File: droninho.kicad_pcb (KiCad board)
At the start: 2 copper layers, 48 x 81.6 mm, 22 parts, among them J1 Conn_01x02_Pin, J2 M2, J3 M1, J4 M3, J5 M4, J6 I2C, J7 TXD0/RXD0, J8 I2C, Q1 SI2300, Q2 SI2300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

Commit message: Ready for review.
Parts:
- removed U3: MPU9250/6500, Library:MPU-9250-6500
- added U4: MPU9250/6500, Library:MPU-9250-6500, F.Cu at (132.1, 136.1)
- J6, J7, J8: footprint Connector:FanPinHeader_1x04_P2.54mm_Vertical -> Connector_PinHeader_2.54mm:PinHeader_1x04_P2.54mm_Vertical
- moved J6 1.51 mm to (127.7, 97.9), turned to 0 degrees
- moved J8 0.93 mm to (162.9, 112.3), turned to 180 degrees
- moved J7 0.89 mm to (162.9, 99.4), turned to 180 degrees
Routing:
- net /SDA: track 89.3 -> 85.4 mm
- net +3.3V: track 215.0 -> 216.1 mm
- net /SCL: track 94.7 -> 93.8 mm
- net GND: track 128.7 -> 129.5 mm
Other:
- board text added: "+3.3v"
- board text added: "- +"
- board text added: "3.3v"
- board text added: "ESP32-DevKit"
- board text added: "GND"
- board text added: "M1"
- board text added: "M2"
- board text added: "M3"
- board text added: "M4"
- board text added: "RX0"
- board text added: "RX2"
- board text added: "RXD2"
- board text added: "SCL"
- board text added: "SDA"
- board text added: "TX0"
- board text added: "TX2"
- board text added: "TXD2"

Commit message: small changes
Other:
- board text removed: "RXD2"
- board text removed: "TXD2"
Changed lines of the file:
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@@
 		)
 	)
-	(gr_text "RXD2"
+	(gr_text "RX2"
 		(at 164.65 110.29 0)
 		(layer "F.SilkS")
@@
 		)
 	)
-	(gr_text "TXD2"
+	(gr_text "TX2"
 		(at 164.65 112.92 0)
 		(layer "F.SilkS")

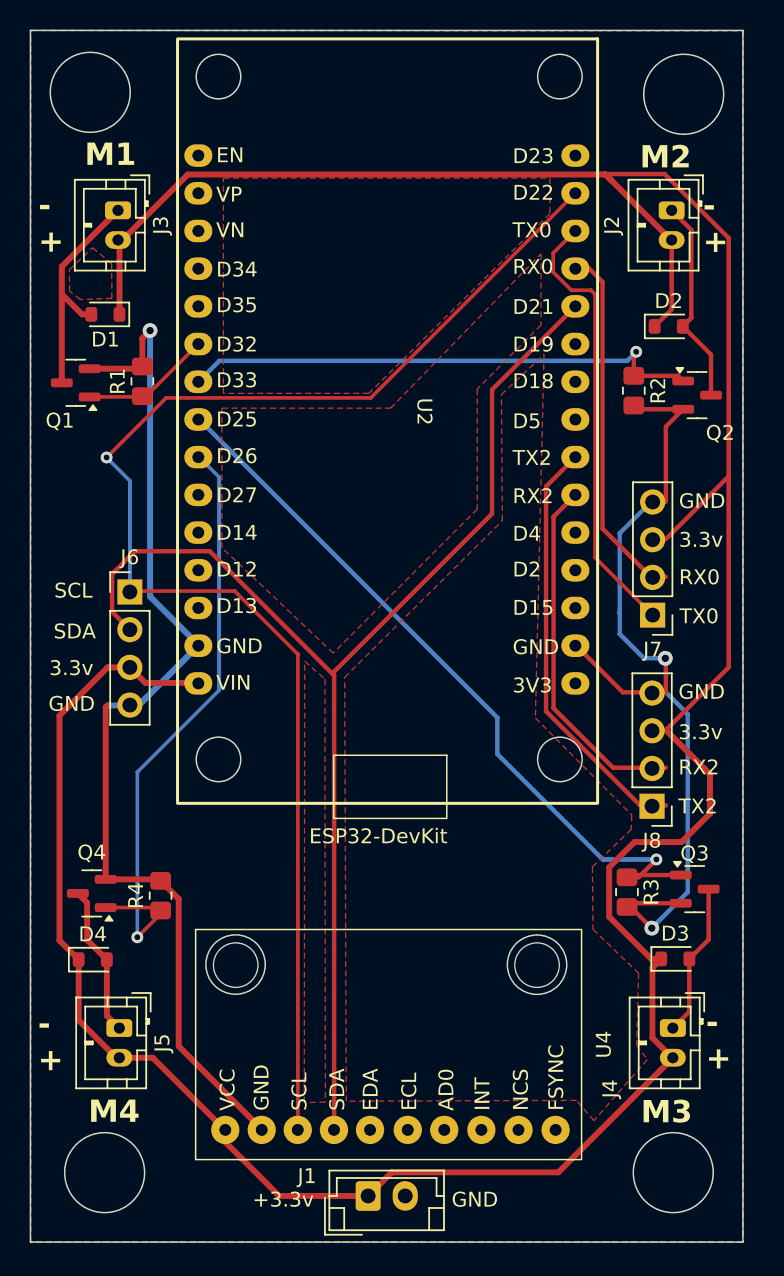
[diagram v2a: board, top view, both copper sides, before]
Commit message: Versão com WIFI de fora da placa.
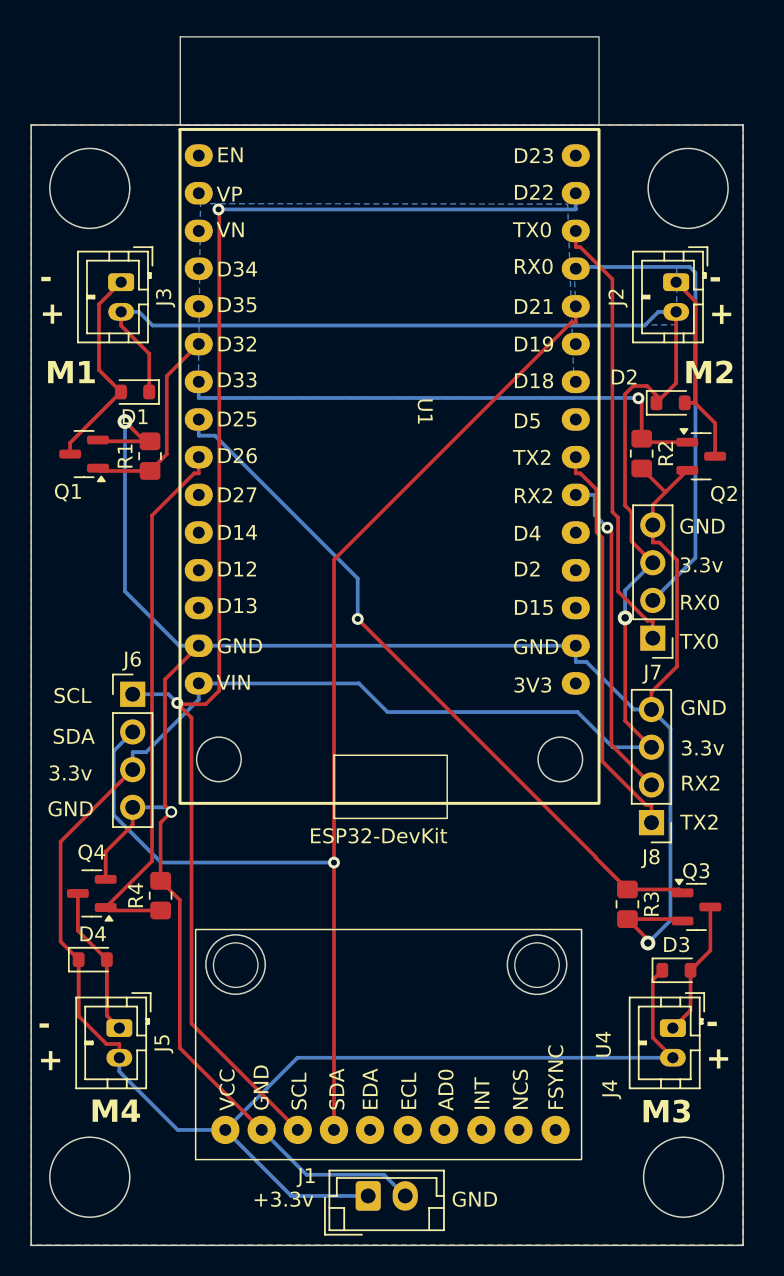
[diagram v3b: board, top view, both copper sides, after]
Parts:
- removed U2: ESP32 Dev Kit, Library:ESP32_30pin
- added U1: ESP32 Dev Kit, Library:ESP32_30pin vertical WIFI, F.Cu at (144.7, 86.2)
- moved J6 6.89 mm to (127.9, 104.8)
- moved D1 5.60 mm to (128.1, 84.4)
- moved D2 5.15 mm to (164.1, 85.1)
- moved R1 5.07 mm to (129.1, 88.7)
- moved J2 4.85 mm to (164.5, 77.0)
- moved J3 4.84 mm to (127.1, 77.0)
- moved Q1 4.83 mm to (124.6, 88.6)
- moved R2 4.27 mm to (162.2, 88.6)
- moved Q2 4.13 mm to (166.2, 88.7)
- moved J7 1.55 mm to (162.9, 101.0)
- moved Q3 1.21 mm to (165.9, 119.1)
- moved J8 1.11 mm to (162.8, 113.4)
- moved R3 0.82 mm to (161.2, 118.9)
- moved D3 0.77 mm to (164.5, 123.4)
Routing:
- net GND: track 129.5 -> 157.3 mm
- net +3.3V: track 216.1 -> 204.3 mm, vias 0 -> 1
- net /RXD0: track 24.4 -> 31.5 mm
- net /PWM1: track 8.84 -> 13.5 mm
- net /PWM4: track 41.5 -> 36.9 mm, vias 1 -> 0
- net /PWM3: track 50.7 -> 48.1 mm
- net /SCL: track 93.8 -> 96.0 mm, vias 1 -> 2
- net /RXD2: track 24.3 -> 22.4 mm, vias 0 -> 1
- net /TXD2: track 28.7 -> 27.1 mm
- net /M1-: track 15.7 -> 14.2 mm
- net /PWM2: track 35.5 -> 36.9 mm
- net /M3-: track 10.4 -> 9.21 mm
- net /SDA: track 85.4 -> 84.7 mm, vias 0 -> 1
- added copper zone on B.Cu, net (none)
- removed copper zone on F.Cu, net (none)
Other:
- board size 48 x 81.6 mm -> 48 x 75.5 mm

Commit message: BOM, DCR e erc OKAY.
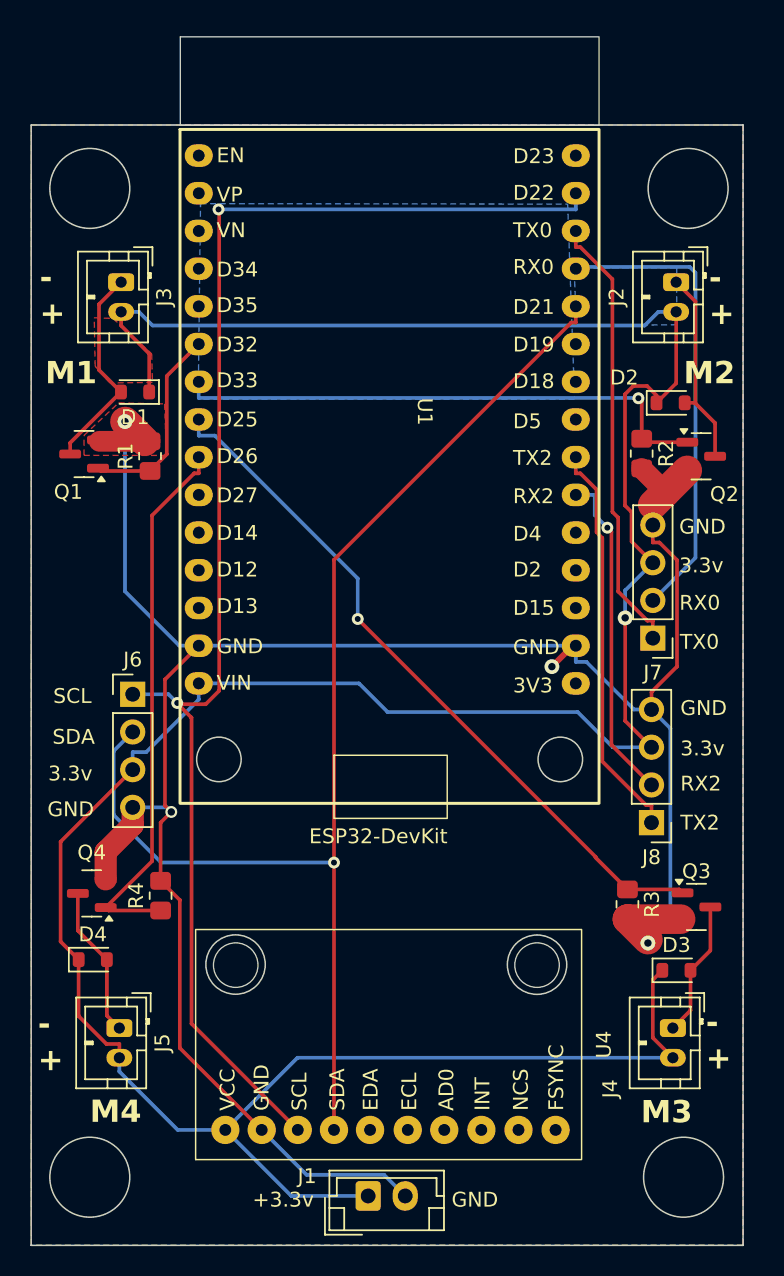
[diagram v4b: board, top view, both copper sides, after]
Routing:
- net GND: track 157.3 -> 159.5 mm, vias 3 -> 4
- added copper zone on F.Cu, net (none)
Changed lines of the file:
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@@
 		(start 162.6 121.3)
 		(end 161.22 119.92)
-		(width 0.25)
+		(width 2)
 		(layer "F.Cu")
 		(net 5)
@@
 		(start 127.89 112.39)
 		(end 127.89 113.5667)
-		(width 0.25)
+		(width 1.5)
 		(layer "F.Cu")
 		(net 5)
@@
 		(start 163.78 91.16)
 		(end 162.18 89.56)
-		(width 0.25)
+		(width 1.4)
 		(layer "F.Cu")
 		(net 5)
@@
 	)
 	(segment
+		(start 157.739987 101.500013)
+		(end 157.76 101.48)
+		(width 0.4)
+		(layer "F.Cu")
+		(net 5)
+	)
+	(segment
 		(start 128.7 87.73)
 		(end 127.37 86.4)
-		(width 0.25)
+		(width 2)
 		(layer "F.Cu")
 		(net 5)
@@
 		(start 125.64 87.73)
 		(end 129.06 87.73)
-		(width 0.25)
+		(width 1.4)
 		(layer "F.Cu")
 		(net 5)
@@
 		(start 127.89 113.5667)
 		(end 126.07 115.3867)
-		(width 0.25)
+		(width 1.5)
 		(layer "F.Cu")
 		(net 5)
@@
 	)
 	(segment
+		(start 157.73996 101.500013)
+		(end 157.539987 101.500013)
+		(width 0.4)
+		(layer "F.Cu")
+		(net 5)
+	)
+	(segment
 		(start 164.5584 95.733863)
 		(end 163.371237 94.5467)
@@
 	)
 	(segment
+		(start 157.73996 101.500013)
+		(end 157.739987 101.500013)
+		(width 0.4)
+		(layer "F.Cu")
+		(net 5)
+	)
+	(segment
 		(start 130.064 103.775973)
 		(end 130.064 112.274)
@@
 		(start 165.25 89.69)
 		(end 163.78 91.16)
-		(width 0.25)
+		(width 2)
 		(layer "F.Cu")
 		(net 5)
@@
 		(start 164.8 119.92)
 		(end 161.22 119.92)
-		(width 0.25)
+		(width 2)
 		(layer "F.Cu")
 		(net 5)
@@
 		(start 163.78 91.16)
 		(end 162.93 92.01)
-		(width 0.25)
+		(width 2)
 		(layer "F.Cu")
 		(net 5)
@@
 		(start 126.07 115.3867)
 		(end 126.07 117.24)
-		(width 0.25)
-		(layer "F.Cu")
+		(width 1.5)
+		(layer "F.Cu")
+		(net 5)
+	)
+	(segment
+		(start 157.539987 101.500013)
+		(end 156.13 102.91)
+		(width 0.4)
+		(layer "F.Cu")
+		(net 5)
+	)
+	(via
+		(at 156.13 102.91)
+		(size 1)
+		(drill 0.5)
+		(layers "F.Cu" "B.Cu")
 		(net 5)
 	)
@@
 	)
 	(zone
+		(net 5)
+		(net_name "GND")
+		(layer "F.Cu")
+		(hatch edge 0.5)
+		(priority 4)
+		(connect_pads
+			(clearance 0.508)
+		)
+		(min_thickness 0.25)
+		(filled_areas_thickness no)
+		(fill yes
+			(thermal_gap 0.5)
+			(thermal_bridge_width 0.5)
+		)
+		(polygon
+			(pts
+				(xy 130.17 88.68) (xy 124.6125 88.6775) (xy 124.6125 87.33) (xy 126.94 85.14) (xy 130.04 85.21)
+			)
+		)
+	)
+	(zone
+		(net 0)
+		(net_name "")
+		(layer "F.Cu")
+		(hatch edge 0.5)
+		(priority 3)
+		(connect_pads
+			(clearance 0.508)
+		)
+		(min_thickness 0.25)
+		(filled_areas_thickness no)
+		(fill yes
+			(thermal_gap 0.5)
+			(thermal_bridge_width 0.5)
+			(island_removal_mode 1)
+			(island_area_min 10)
+		)
+		(polygon
+			(pts
+				(xy 125.3 79.41) (xy 126.56 79.45) (xy 129.17 81.84) (xy 129.22 83.76) (xy 126.36 83.8) (xy 125.36 82.67)
+			)
+		)
+	)
+	(zone

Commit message: Correções em footprints e troca de lado do ESP32.
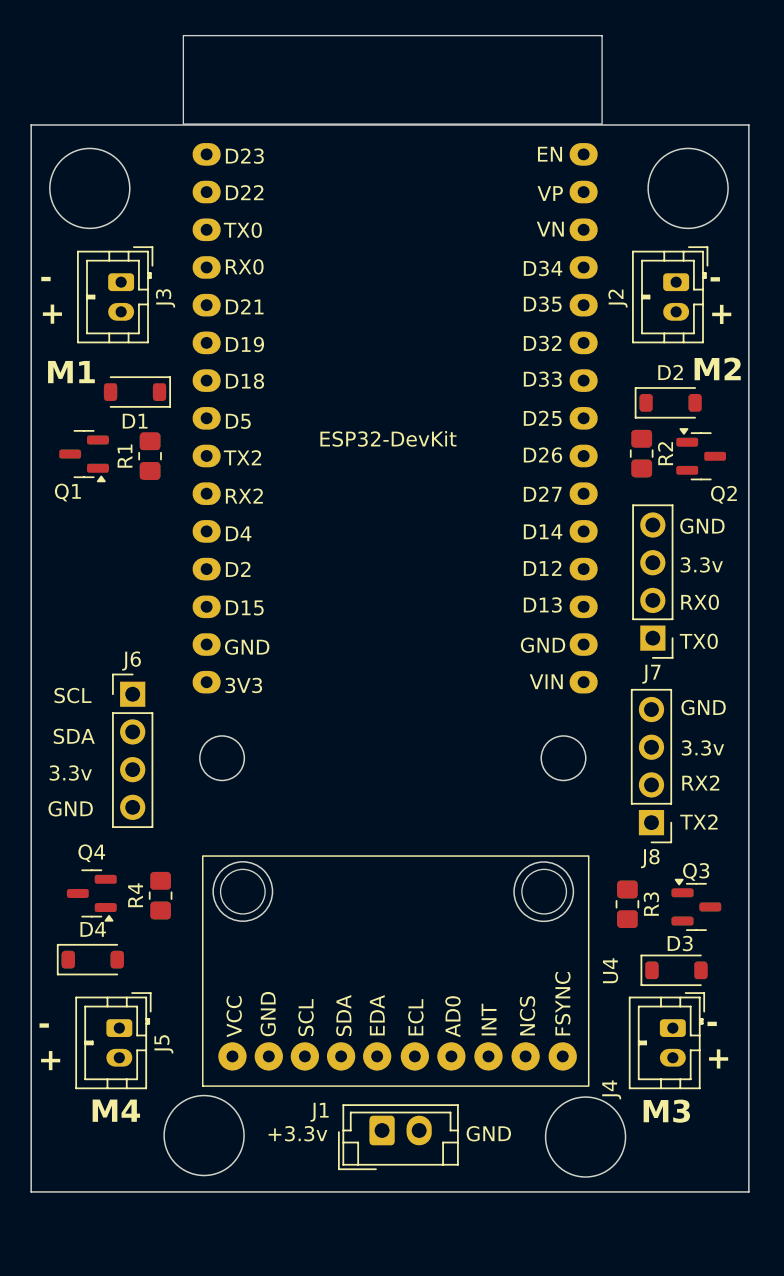
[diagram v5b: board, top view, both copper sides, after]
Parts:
- D1, D2, D3, D4: footprint Diode_SMD:D_SOD-110 -> Diode_SMD:D_SOD-123
- U1: moved to B.Cu
- moved U4 4.97 mm to (132.6, 131.2)
- moved J1 4.51 mm to (144.7, 134.2)
- moved U1 1.14 mm to (145.9, 86.1), turned to 180 degrees
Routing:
- net +3.3V: track 204.3 -> 0.00 mm, vias 1 -> 0
- net GND: track 159.5 -> 0.00 mm, vias 4 -> 0
- net /SCL: track 96.0 -> 0.00 mm, vias 2 -> 0
- net /SDA: track 84.7 -> 0.00 mm, vias 1 -> 0
- net /PWM3: track 48.1 -> 0.00 mm, vias 1 -> 0
- net /PWM2: track 36.9 -> 0.00 mm, vias 1 -> 0
- net /PWM4: track 36.9 -> 0.00 mm
- net /RXD0: track 31.5 -> 0.00 mm
- net /TXD0: track 30.0 -> 0.00 mm
- net /TXD2: track 27.1 -> 0.00 mm
- net /RXD2: track 22.4 -> 0.00 mm, vias 1 -> 0
- net /M1-: track 14.2 -> 0.00 mm
- net /M2-: track 13.5 -> 0.00 mm
- net /PWM1: track 13.5 -> 0.00 mm
- net /M4-: track 10.2 -> 0.00 mm
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- removed copper zone on B.Cu, net (none)
- removed copper zone on F.Cu, net (none)
- removed copper zone on B.Cu, net GND
- removed copper zone on F.Cu, net GND
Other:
- board size 48 x 75.5 mm -> 48.4 x 71.9 mm
- board text added: "MPU925/6500"
